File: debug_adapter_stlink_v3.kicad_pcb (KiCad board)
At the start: 2 copper layers, 51.9 x 20 mm, 5 parts, among them J1 Conn_ST_STDC14, J2 DebugEdge_02x05, J3 Conn_02x05_Odd_Even, J4 Conn_01x02_Male

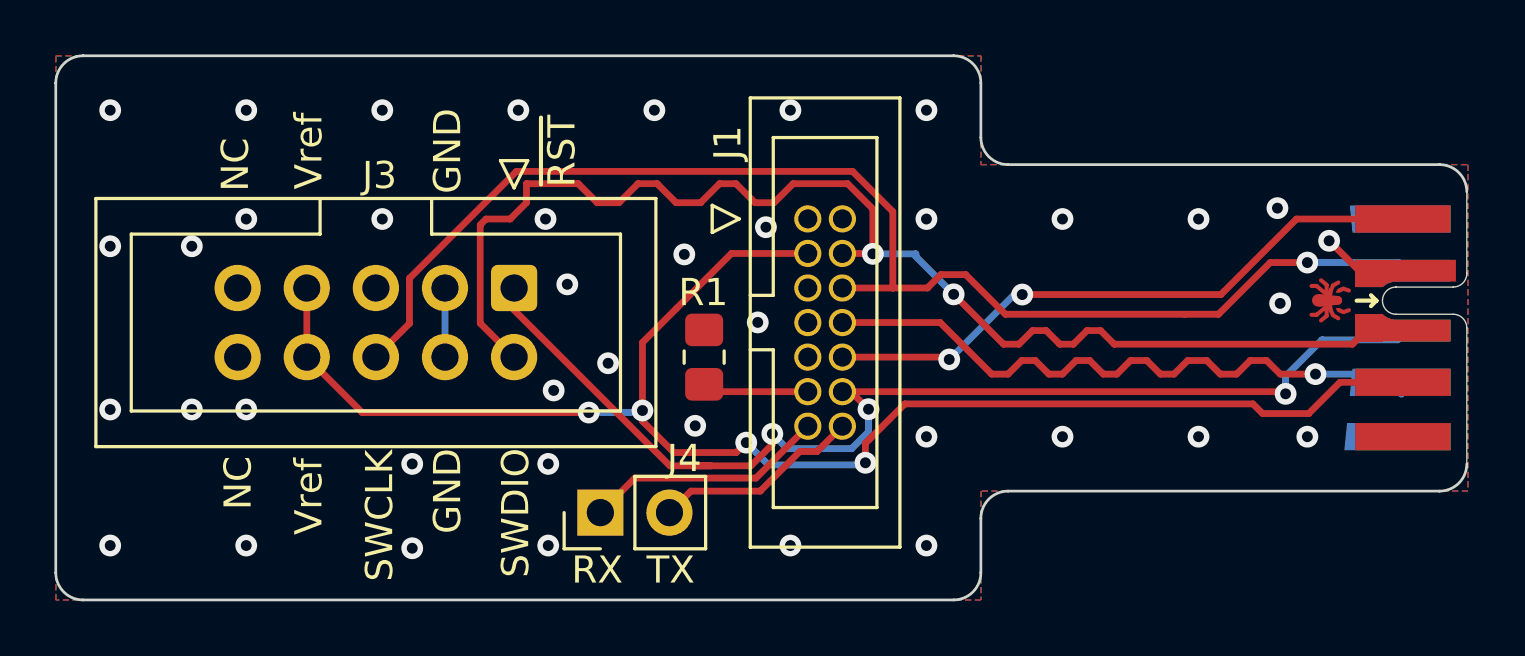
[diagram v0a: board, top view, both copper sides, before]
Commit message: Remove the ST-Link-v2-clone connector
Reason: The adaptor for the ST-Link-V2 clone connector will be
implemented as its own PCB.
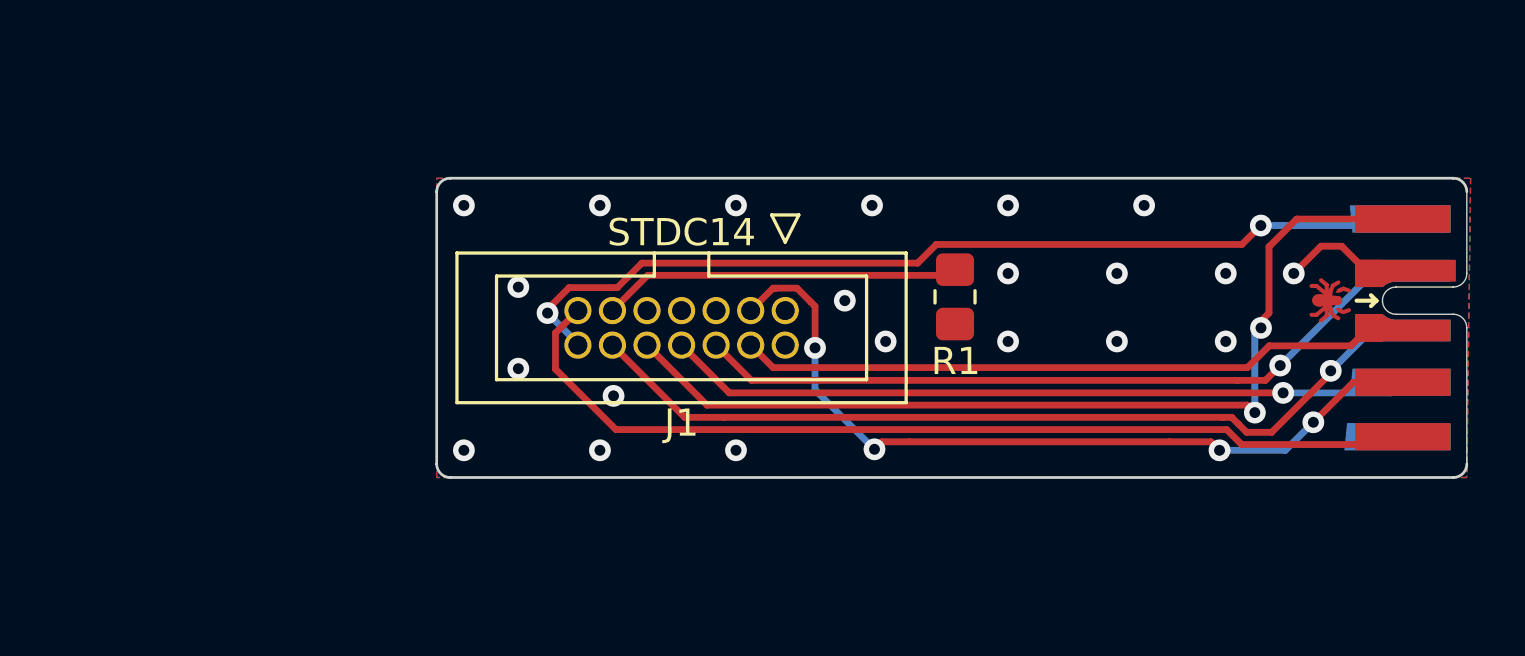
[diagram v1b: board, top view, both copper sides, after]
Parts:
- removed J3: Conn_02x05_Odd_Even, Connector_IDC:IDC-Header_2x05_P2.54mm_Vertical
- removed J4: Conn_01x02_Male, Connector_PinHeader_2.54mm:PinHeader_1x02_P2.54mm_Vertical
- moved R1 9.48 mm to (173.1, 89.9), turned to 90 degrees
- moved J1 5.28 mm to (163.0, 91.0), turned to 0 degrees
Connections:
- J2 pad 8: unconnected-(J2-Pad8) -> /VCP_TX
- J2 pad 9: unconnected-(J2-Pad9) -> /VCP_RX
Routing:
- net /Vref: track 57.0 -> 29.8 mm
- net /VCP_TX: track 7.67 -> 34.5 mm, vias 0 -> 2
- net /VCP_RX: track 8.94 -> 34.9 mm
- net /SWDIO: track 46.5 -> 23.7 mm, vias 2 -> 0
- net /SWCLK: track 48.8 -> 27.7 mm
- net /JTDI: track 22.8 -> 35.0 mm
- net /~{RST}: track 42.4 -> 32.3 mm, vias 3 -> 1
- net Net-(J1-Pad11): track 3.92 -> 13.2 mm
- net /JTDO: track 23.7 -> 27.3 mm
- net GND: track 4.50 -> 3.59 mm, vias 40 -> 21
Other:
- board size 51.9 x 20 mm -> 37.9 x 11 mm
- board text added: "STDC14"
- board text removed: "GND"
- board text removed: "NC"
- board text removed: "RX"
- board text removed: "SWCLK"
- board text removed: "SWDIO"
- board text removed: "TX"
- board text removed: "Vref"
- board text removed: "~{RST}"
